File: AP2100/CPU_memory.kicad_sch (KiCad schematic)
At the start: 70 parts, among them IC3 AS4C256M16D4-75BCN, IC4 AS4C256M16D4-75BCN, U1 LS1043ASE7KQB

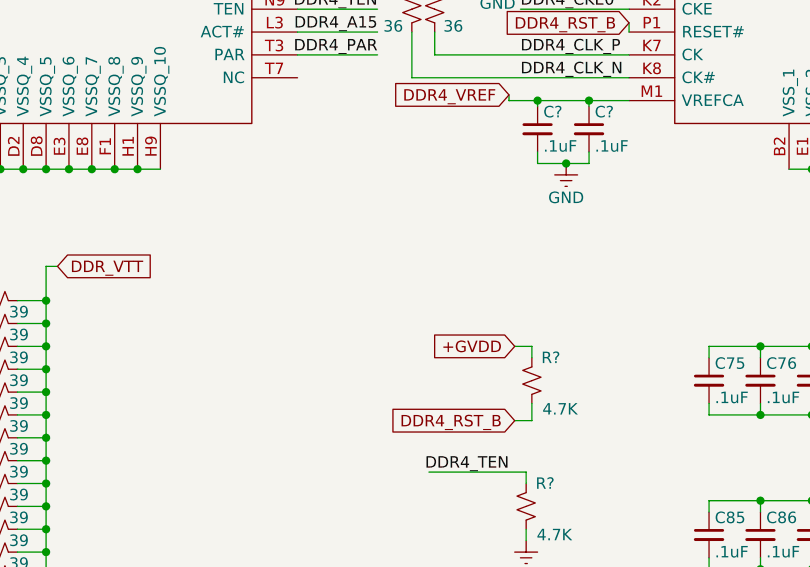
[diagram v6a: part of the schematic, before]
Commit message: Add 1.2V and 5V power supplies
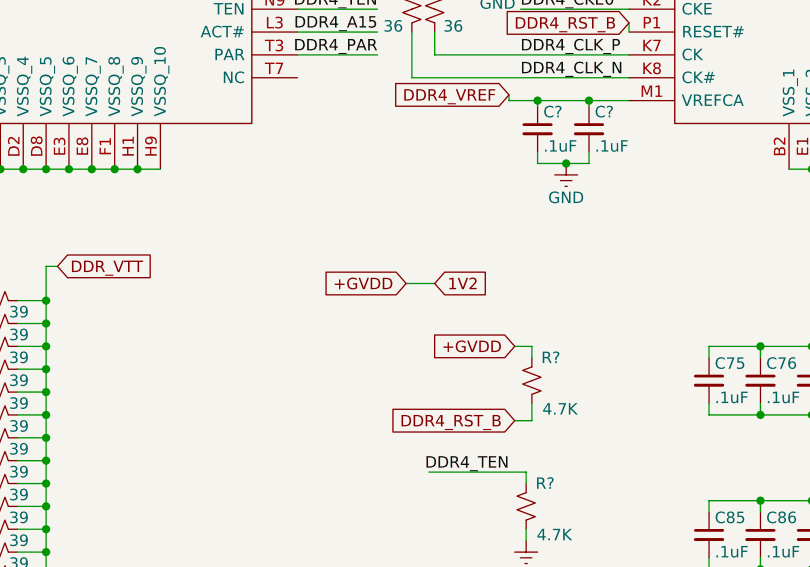
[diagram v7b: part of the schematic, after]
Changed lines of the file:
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@@
-(kicad_sch (version 20200827) (generator eeschema)
+(kicad_sch (version 20200828) (generator eeschema)
   (page 2 6)
   (paper "USLegal")
@@
   (junction (at 318.77 23.495) (diameter 0.9144) (color 0 0 0 0))
   (junction (at 318.77 31.115) (diameter 0.9144) (color 0 0 0 0))
+  (no_connect (at 80.01 179.07))
+  (no_connect (at 29.21 161.29))
+  (no_connect (at 80.01 120.65))
+  (no_connect (at 80.01 184.15))
+  (no_connect (at 80.01 107.95))
+  (no_connect (at 29.21 163.83))
+  (no_connect (at 29.21 49.53))
   (no_connect (at 80.01 105.41))
-  (no_connect (at 80.01 179.07))
-  (no_connect (at 80.01 184.15))
+  (no_connect (at 80.01 49.53))
+  (no_connect (at 80.01 176.53))
   (no_connect (at 80.01 181.61))
-  (no_connect (at 80.01 49.53))
-  (no_connect (at 29.21 49.53))
-  (no_connect (at 80.01 176.53))
-  (no_connect (at 80.01 107.95))
   (no_connect (at 80.01 118.11))
-  (no_connect (at 29.21 161.29))
-  (no_connect (at 29.21 163.83))
-  (no_connect (at 80.01 120.65))
   (wire (pts (xy 13.97 184.15) (xy 20.32 184.15))
     (stroke (width 0) (type solid) (color 0 0 0 0))
@@
   )
   (wire (pts (xy 200.66 103.505) (xy 209.55 103.505))
+    (stroke (width 0) (type solid) (color 0 0 0 0))
+  )
+  (wire (pts (xy 212.725 128.905) (xy 215.9 128.905))
     (stroke (width 0) (type solid) (color 0 0 0 0))
   )
@@
     (effects (font (size 1.27 1.27)) (justify left))
   )
+  (global_label "+GVDD" (shape input) (at 212.725 128.905 180)
+    (effects (font (size 1.27 1.27)) (justify right))
+  )
   (global_label "+GVDD" (shape input) (at 214.63 86.995 0)
     (effects (font (size 1.27 1.27)) (justify left))
   )
+  (global_label "1V2" (shape input) (at 215.9 128.905 0)
+    (effects (font (size 1.27 1.27)) (justify left))
+  )
